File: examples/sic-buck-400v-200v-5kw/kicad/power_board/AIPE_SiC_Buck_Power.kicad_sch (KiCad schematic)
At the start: 0 parts

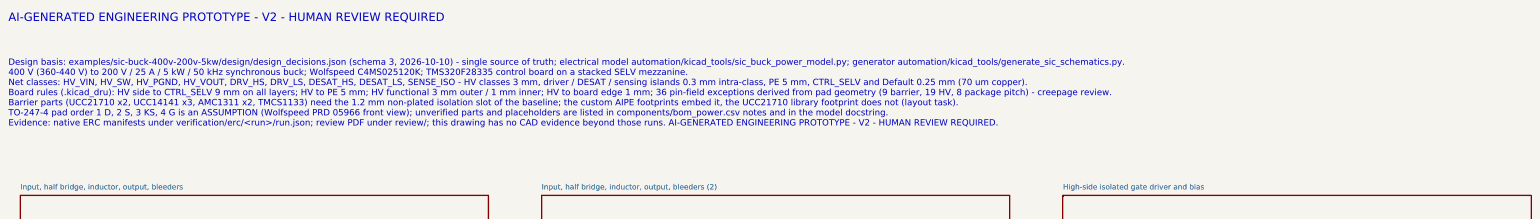
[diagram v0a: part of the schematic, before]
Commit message: fix(pcb): structural DRC sources removed at the schematic level; layout review and stage-3 evidence
Power project regenerated (ERC 0 findings, run 20261010T165532Z): UCC21710 drivers now use
an AIPE footprint that carries its own 1.2 x 16.6 mm isolation slot (no library
silkscreen crossing a board cut-out), the AMC1311 slot is lengthened to 10.8 mm, the
LED anode nodes of the indicator strings form a PGND_LV class of the PGND reference
island (0.3 mm to PGND instead of a 3 mm HV spacing an 0805 LED cannot meet), and the
pin-field exceptions now cover no-connect pads whose unconnected-* nets fall into
KiCad's Default class. 45 design rules; nothing weakened.

Also records the independent layout review of the first routed state
(pcb_rule_review.md, 19 findings), the correction pass before/after tables, the
stage-3 power-board routing experiments and patch set, the stage-1 floorplan
generator with its candidate comparison, run_check report hashes and the verifier
hash fix.

Co-Authored-By: Claude Fable 5.1 <noreply@anthropic.com>
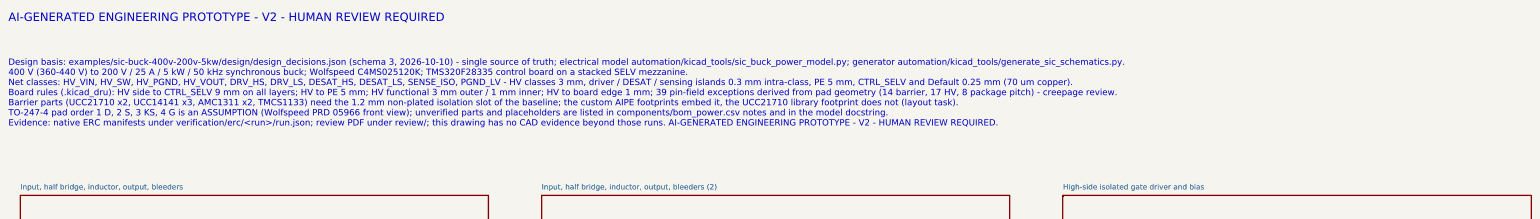
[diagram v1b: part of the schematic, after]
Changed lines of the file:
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@@
           (effects (font (size 2 2)) (justify left top))
 )
-(text "Design basis: examples/sic-buck-400v-200v-5kw/design/design_decisions.json (schema 3, 2026-10-10) - single source of truth; electrical model automation/kicad_tools/sic_buck_power_model.py; generator automation/kicad_tools/generate_sic_schematics.py.\n400 V (360-440 V) to 200 V / 25 A / 5 kW / 50 kHz synchronous buck; Wolfspeed C4MS025120K; TMS320F28335 control board on a stacked SELV mezzanine.\nNet classes: HV_VIN, HV_SW, HV_PGND, HV_VOUT, DRV_HS, DRV_LS, DESAT_HS, DESAT_LS, SENSE_ISO - HV classes 3 mm, driver / DESAT / sensing islands 0.3 mm intra-class, PE 5 mm, CTRL_SELV and Default 0.25 mm (70 um copper).\nBoard rules (.kicad_dru): HV side to CTRL_SELV 9 mm on all layers; HV to PE 5 mm; HV functional 3 mm outer / 1 mm inner; HV to board edge 1 mm; 36 pin-field exceptions derived from pad geometry (9 barrier, 19 HV, 8 package pitch) - creepage review.\nBarrier parts (UCC21710 x2, UCC14141 x3, AMC1311 x2, TMCS1133) need the 1.2 mm non-plated isolation slot of the baseline; the custom AIPE footprints embed it, the UCC21710 library footprint does not (layout task).\nTO-247-4 pad order 1 D, 2 S, 3 KS, 4 G is an ASSUMPTION (Wolfspeed PRD 05966 front view); unverified parts and placeholders are listed in components/bom_power.csv notes and in the model docstring.\nEvidence: native ERC manifests under verification/erc/<run>/run.json; review PDF under review/; this drawing has no CAD evidence beyond those runs. AI-GENERATED ENGINEERING PROTOTYPE - V2 - HUMAN REVIEW REQUIRED." (at 20 31 0)
+(text "Design basis: examples/sic-buck-400v-200v-5kw/design/design_decisions.json (schema 3, 2026-10-10) - single source of truth; electrical model automation/kicad_tools/sic_buck_power_model.py; generator automation/kicad_tools/generate_sic_schematics.py.\n400 V (360-440 V) to 200 V / 25 A / 5 kW / 50 kHz synchronous buck; Wolfspeed C4MS025120K; TMS320F28335 control board on a stacked SELV mezzanine.\nNet classes: HV_VIN, HV_SW, HV_PGND, HV_VOUT, DRV_HS, DRV_LS, DESAT_HS, DESAT_LS, SENSE_ISO, PGND_LV - HV classes 3 mm, driver / DESAT / sensing islands 0.3 mm intra-class, PE 5 mm, CTRL_SELV and Default 0.25 mm (70 um copper).\nBoard rules (.kicad_dru): HV side to CTRL_SELV 9 mm on all layers; HV to PE 5 mm; HV functional 3 mm outer / 1 mm inner; HV to board edge 1 mm; 39 pin-field exceptions derived from pad geometry (14 barrier, 17 HV, 8 package pitch) - creepage review.\nBarrier parts (UCC21710 x2, UCC14141 x3, AMC1311 x2, TMCS1133) need the 1.2 mm non-plated isolation slot of the baseline; the custom AIPE footprints embed it, the UCC21710 library footprint does not (layout task).\nTO-247-4 pad order 1 D, 2 S, 3 KS, 4 G is an ASSUMPTION (Wolfspeed PRD 05966 front view); unverified parts and placeholders are listed in components/bom_power.csv notes and in the model docstring.\nEvidence: native ERC manifests under verification/erc/<run>/run.json; review PDF under review/; this drawing has no CAD evidence beyond those runs. AI-GENERATED ENGINEERING PROTOTYPE - V2 - HUMAN REVIEW REQUIRED." (at 20 31 0)
           (effects (font (size 1.5 1.5)) (justify left top))
 )

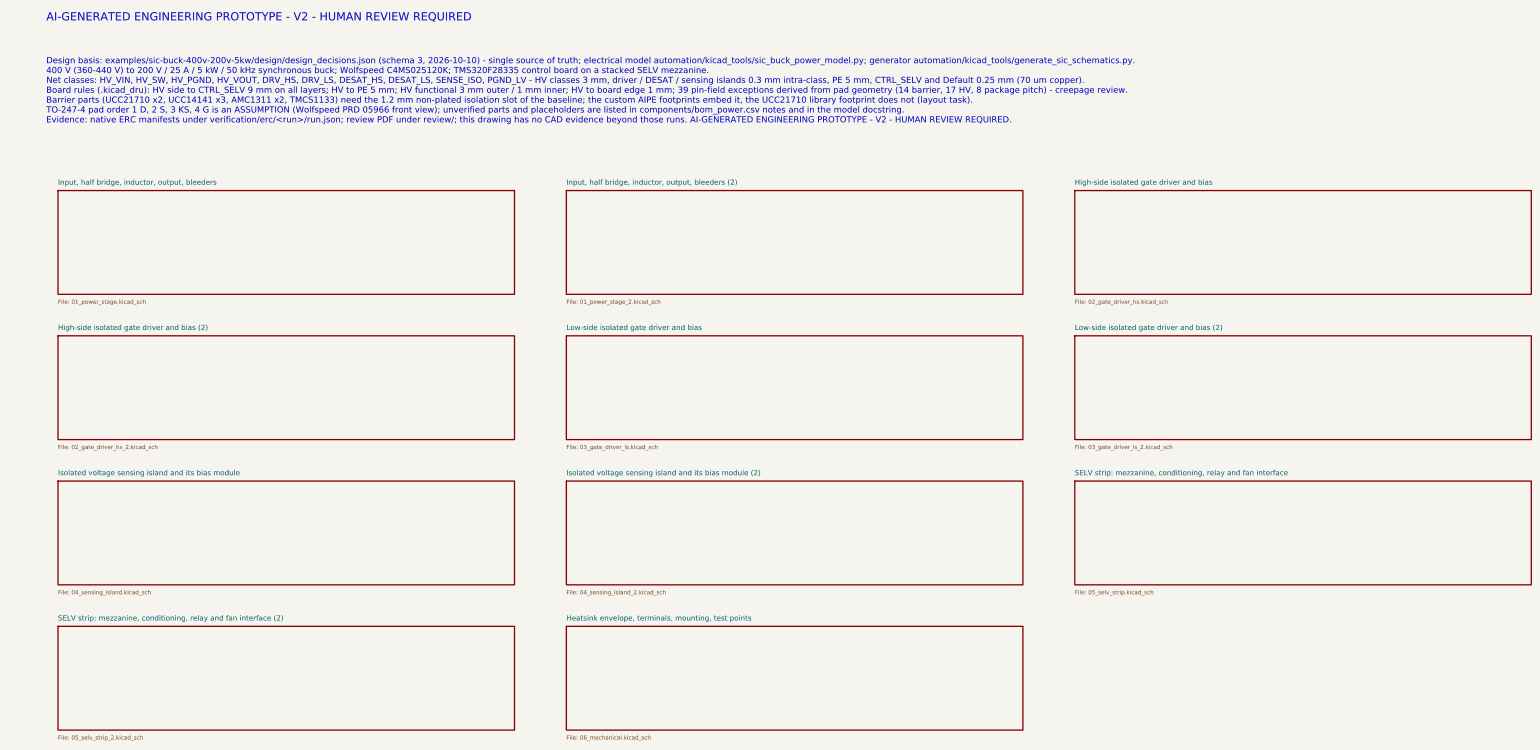
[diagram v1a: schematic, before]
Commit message: feat(v2.1): example regenerated - wired schematics, both boards routed with the upgraded router, exports, crops, validation
Schematics (wired style, gates passed): ERC 0 on both projects (power 20261012T075113Z-erc-df18ce6e,
control 20261012T075120Z-erc-7a14cacb); netlist (ref,pad)->net exact vs the model and vs the frozen V2
netlists with equal net names; .kicad_dru / net_settings identical to the legacy generation; stub
global labels 648 -> 7 (power) and 667 -> 7 (control), wired pin share 0 -> 0.90 / 0.76, junctions,
hierarchical labels and power symbols introduced, continuation sheets removed; readability metrics
V2 vs V2.1 in engineering_checks/schematic_readability_*.

Power board (octilinear simplification + tangent arcs on the V2 search; 8-direction search kept
opt-in after attempt A left 2 connections open): 0 unresolved, DRC 0/0/0 (20261012T090308Z-drc-8fd50803),
segments 4755 -> 2991 + 145 arcs, 90-degree bends 3609 -> 1121, stair runs 382 -> 124, length
5744.6 -> 5545.6 mm, vias 606 = V2, no net longer / more vias / narrower. Control board: 0 unresolved,
DRC 0/0/0 (20261012T084327Z-drc-7f07f983), segments 5995 -> 4262 + 261 arcs, 90-degree bends
4069 -> 1233, stair runs 435 -> 144, length 7055.2 -> 6700.7 mm, vias 798 = V2, 96 nets shorter,
0 longer. FOOTPRINT.SetDNP for DNP parts (schematic parity), beautify anchors bound to off-grid vias
by copper overlap (path_geometry.connected_by_overlap), In2.Cu inner pass styled.

Exports 11/11 per board, renders and layer PDFs refreshed, high-resolution V2/V2.1 crops under
review/crops/, routing_quality_* and v21_validation.{json,md} (nine TASK 7 checks independently
re-derived). verify_sic_buck passed; 338 tests OK (2 skipped).

Co-Authored-By: Claude Fable 5.1 <noreply@anthropic.com>
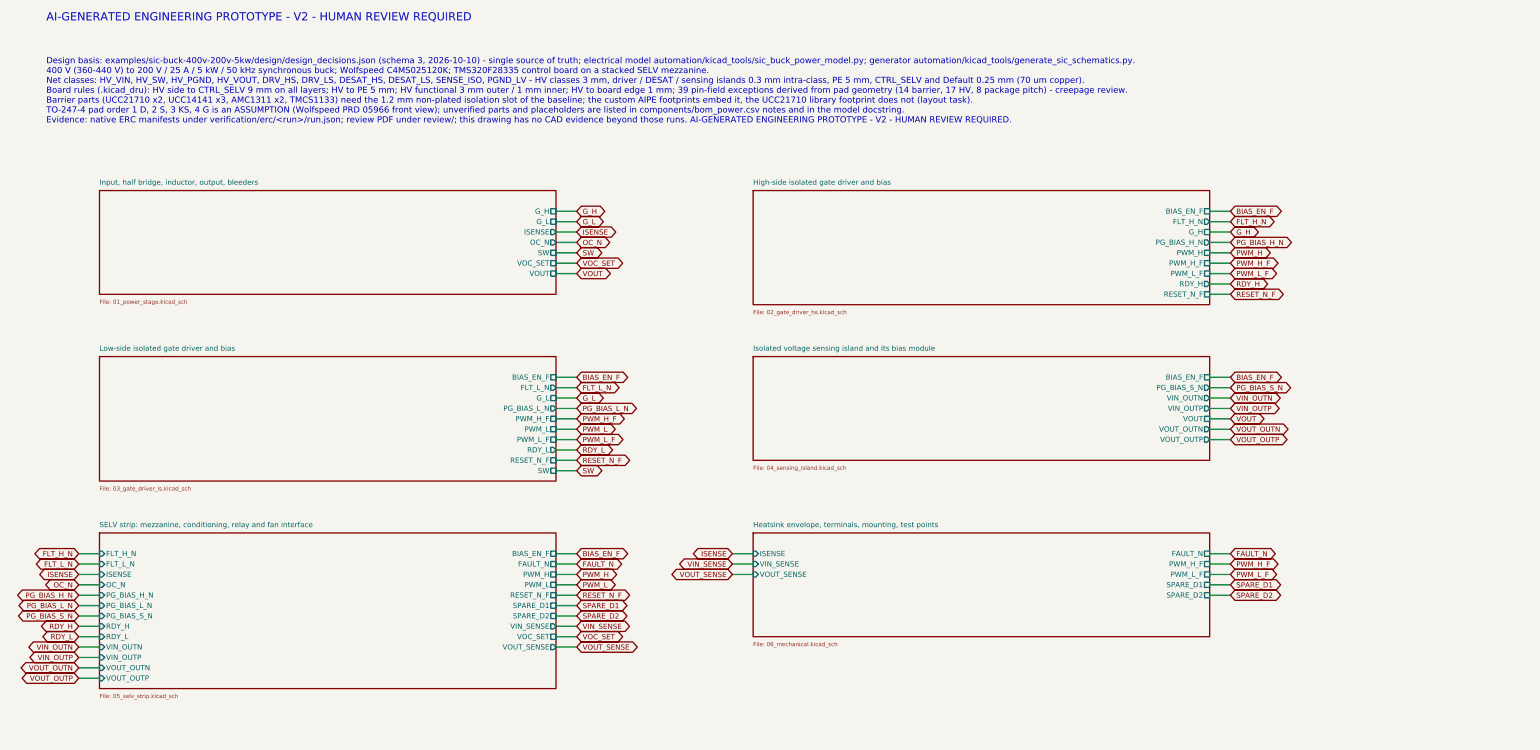
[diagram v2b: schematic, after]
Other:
- removed sheet High-side isolated gate driver and bias (2)
- removed sheet Input, half bridge, inductor, output, bleeders (2)
- removed sheet Isolated voltage sensing island and its bias module (2)
- removed sheet Low-side isolated gate driver and bias (2)
- removed sheet SELV strip: mezzanine, conditioning, relay and fan interface (2)
- sheet Heatsink envelope, terminals, mounting, test points ports: added FAULT_N, ISENSE, PWM_H_F, PWM_L_F, SPARE_D1, SPARE_D2, VIN_SENSE, VOUT_SENSE; removed none
- sheet High-side isolated gate driver and bias ports: added BIAS_EN_F, FLT_H_N, G_H, PG_BIAS_H_N, PWM_H, PWM_H_F, PWM_L_F, RDY_H, RESET_N_F; removed none
- sheet Input, half bridge, inductor, output, bleeders ports: added G_H, G_L, ISENSE, OC_N, SW, VOC_SET, VOUT; removed none
- sheet Isolated voltage sensing island and its bias module ports: added BIAS_EN_F, PG_BIAS_S_N, VIN_OUTN, VIN_OUTP, VOUT, VOUT_OUTN, VOUT_OUTP; removed none
- sheet Low-side isolated gate driver and bias ports: added BIAS_EN_F, FLT_L_N, G_L, PG_BIAS_L_N, PWM_H_F, PWM_L, PWM_L_F, RDY_L, RESET_N_F, SW; removed none
- sheet SELV strip: mezzanine, conditioning, relay and fan interface ports: added BIAS_EN_F, FAULT_N, FLT_H_N, FLT_L_N, ISENSE, OC_N, PG_BIAS_H_N, PG_BIAS_L_N, PG_BIAS_S_N, PWM_H, PWM_L, RDY_H, RDY_L, RESET_N_F, SPARE_D1, SPARE_D2, VIN_OUTN, VIN_OUTP, VIN_SENSE, VOC_SET, VOUT_OUTN, VOUT_OUTP, VOUT_SENSE; removed none

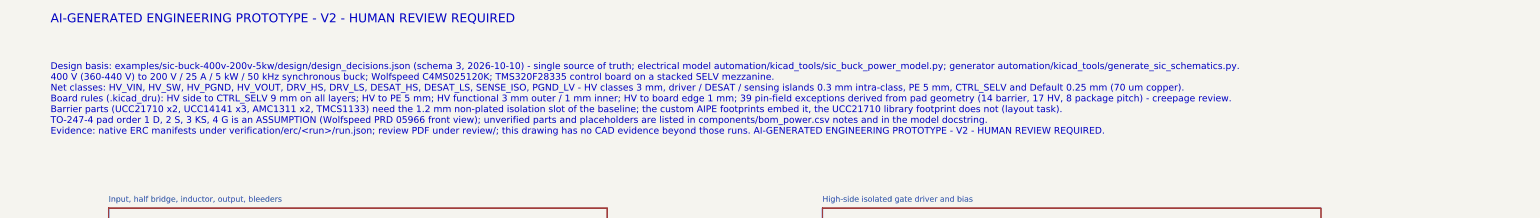
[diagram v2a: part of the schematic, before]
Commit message: chore(v2.1): one generation label (sic_buck_common.GENERATION) and a reproducible full regeneration
GENERATION = "V2.1" derives BANNER, REVISION, title-block comments, .kicad_dru headers,
NOTICE.md, the power-board silkscreen and the control-board label (kept at the V2 label
length so the placer's text obstacle box, and therefore the placement, is unchanged).
Models, schematics (ERC 0: 20261012T094955Z-erc-c574a866 / 20261012T095007Z-erc-caa10a79,
all gates passed), both boards (DRC 0/0/0: power 20261012T100423Z-drc-8b9e64d1, control
20261012T103755Z-drc-0a4fa5cf), netlist checks, routing-quality records (totals, per-layer
and per-net tables identical to the previous commit), exports (11/11 each), renders, V2.1
crops (same framing; V2 crops untouched) and readability reports regenerated. Independent
re-validation in verification/v21_validation.{json,md} (12 rows). verify_sic_buck passed;
340 tests OK (2 skipped). Known residue: control-board corridor zone priorities depend on
reload order (same zones, DRC clean), manufacturing/README.md still describes the V2 bundle.

Co-Authored-By: Claude Fable 5.1 <noreply@anthropic.com>
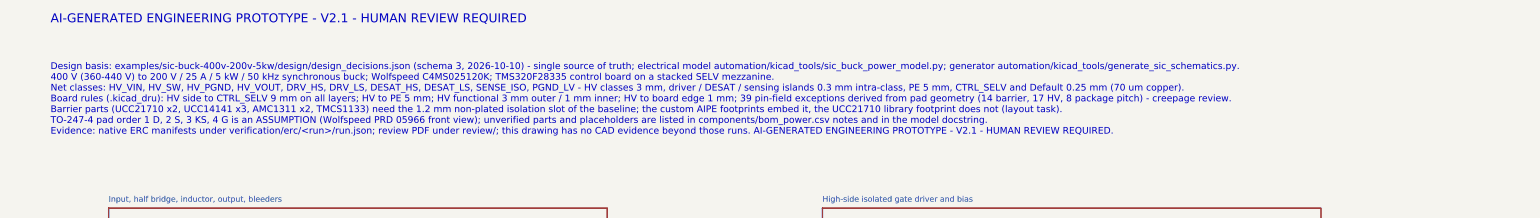
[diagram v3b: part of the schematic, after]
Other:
- note added: "AI-GENERATED ENGINEERING PROTOTYPE - V2.1 - HUMAN REVIEW REQUIRED"
- note removed: "AI-GENERATED ENGINEERING PROTOTYPE - V2 - HUMAN REVIEW REQUIRED"
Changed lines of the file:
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@@
  (paper "A3")
           (title_block (title "AIPE V2 SiC buck power board - 400 V (360-440 V) to 200 V / 25 A / 5 kW / 50 kHz synchronous buck; Wolfspeed C4MS025120K; TMS320F28335 control board on a stacked SELV mezzanine") (rev "V2.1")
-            (comment 1 "AI-GENERATED ENGINEERING PROTOTYPE - V2 - HUMAN REVIEW REQUIRED"))
-          (text "AI-GENERATED ENGINEERING PROTOTYPE - V2 - HUMAN REVIEW REQUIRED" (at 20 20 0)
+            (comment 1 "AI-GENERATED ENGINEERING PROTOTYPE - V2.1 - HUMAN REVIEW REQUIRED"))
+          (text "AI-GENERATED ENGINEERING PROTOTYPE - V2.1 - HUMAN REVIEW REQUIRED" (at 20 20 0)
           (effects (font (size 2 2)) (justify left top))
 )
-(text "Design basis: examples/sic-buck-400v-200v-5kw/design/design_decisions.json (schema 3, 2026-10-10) - single source of truth; electrical model automation/kicad_tools/sic_buck_power_model.py; generator automation/kicad_tools/generate_sic_schematics.py.\n400 V (360-440 V) to 200 V / 25 A / 5 kW / 50 kHz synchronous buck; Wolfspeed C4MS025120K; TMS320F28335 control board on a stacked SELV mezzanine.\nNet classes: HV_VIN, HV_SW, HV_PGND, HV_VOUT, DRV_HS, DRV_LS, DESAT_HS, DESAT_LS, SENSE_ISO, PGND_LV - HV classes 3 mm, driver / DESAT / sensing islands 0.3 mm intra-class, PE 5 mm, CTRL_SELV and Default 0.25 mm (70 um copper).\nBoard rules (.kicad_dru): HV side to CTRL_SELV 9 mm on all layers; HV to PE 5 mm; HV functional 3 mm outer / 1 mm inner; HV to board edge 1 mm; 39 pin-field exceptions derived from pad geometry (14 barrier, 17 HV, 8 package pitch) - creepage review.\nBarrier parts (UCC21710 x2, UCC14141 x3, AMC1311 x2, TMCS1133) need the 1.2 mm non-plated isolation slot of the baseline; the custom AIPE footprints embed it, the UCC21710 library footprint does not (layout task).\nTO-247-4 pad order 1 D, 2 S, 3 KS, 4 G is an ASSUMPTION (Wolfspeed PRD 05966 front view); unverified parts and placeholders are listed in components/bom_power.csv notes and in the model docstring.\nEvidence: native ERC manifests under verification/erc/<run>/run.json; review PDF under review/; this drawing has no CAD evidence beyond those runs. AI-GENERATED ENGINEERING PROTOTYPE - V2 - HUMAN REVIEW REQUIRED." (at 20 31 0)
+(text "Design basis: examples/sic-buck-400v-200v-5kw/design/design_decisions.json (schema 3, 2026-10-10) - single source of truth; electrical model automation/kicad_tools/sic_buck_power_model.py; generator automation/kicad_tools/generate_sic_schematics.py.\n400 V (360-440 V) to 200 V / 25 A / 5 kW / 50 kHz synchronous buck; Wolfspeed C4MS025120K; TMS320F28335 control board on a stacked SELV mezzanine.\nNet classes: HV_VIN, HV_SW, HV_PGND, HV_VOUT, DRV_HS, DRV_LS, DESAT_HS, DESAT_LS, SENSE_ISO, PGND_LV - HV classes 3 mm, driver / DESAT / sensing islands 0.3 mm intra-class, PE 5 mm, CTRL_SELV and Default 0.25 mm (70 um copper).\nBoard rules (.kicad_dru): HV side to CTRL_SELV 9 mm on all layers; HV to PE 5 mm; HV functional 3 mm outer / 1 mm inner; HV to board edge 1 mm; 39 pin-field exceptions derived from pad geometry (14 barrier, 17 HV, 8 package pitch) - creepage review.\nBarrier parts (UCC21710 x2, UCC14141 x3, AMC1311 x2, TMCS1133) need the 1.2 mm non-plated isolation slot of the baseline; the custom AIPE footprints embed it, the UCC21710 library footprint does not (layout task).\nTO-247-4 pad order 1 D, 2 S, 3 KS, 4 G is an ASSUMPTION (Wolfspeed PRD 05966 front view); unverified parts and placeholders are listed in components/bom_power.csv notes and in the model docstring.\nEvidence: native ERC manifests under verification/erc/<run>/run.json; review PDF under review/; this drawing has no CAD evidence beyond those runs. AI-GENERATED ENGINEERING PROTOTYPE - V2.1 - HUMAN REVIEW REQUIRED." (at 20 31 0)
           (effects (font (size 1.5 1.5)) (justify left top))
 )
